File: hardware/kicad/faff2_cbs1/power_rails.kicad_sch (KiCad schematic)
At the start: 58 parts, among them U301 LMR33630, U302 TPS7A20, U303 TPS7A20, U304 LMR33630

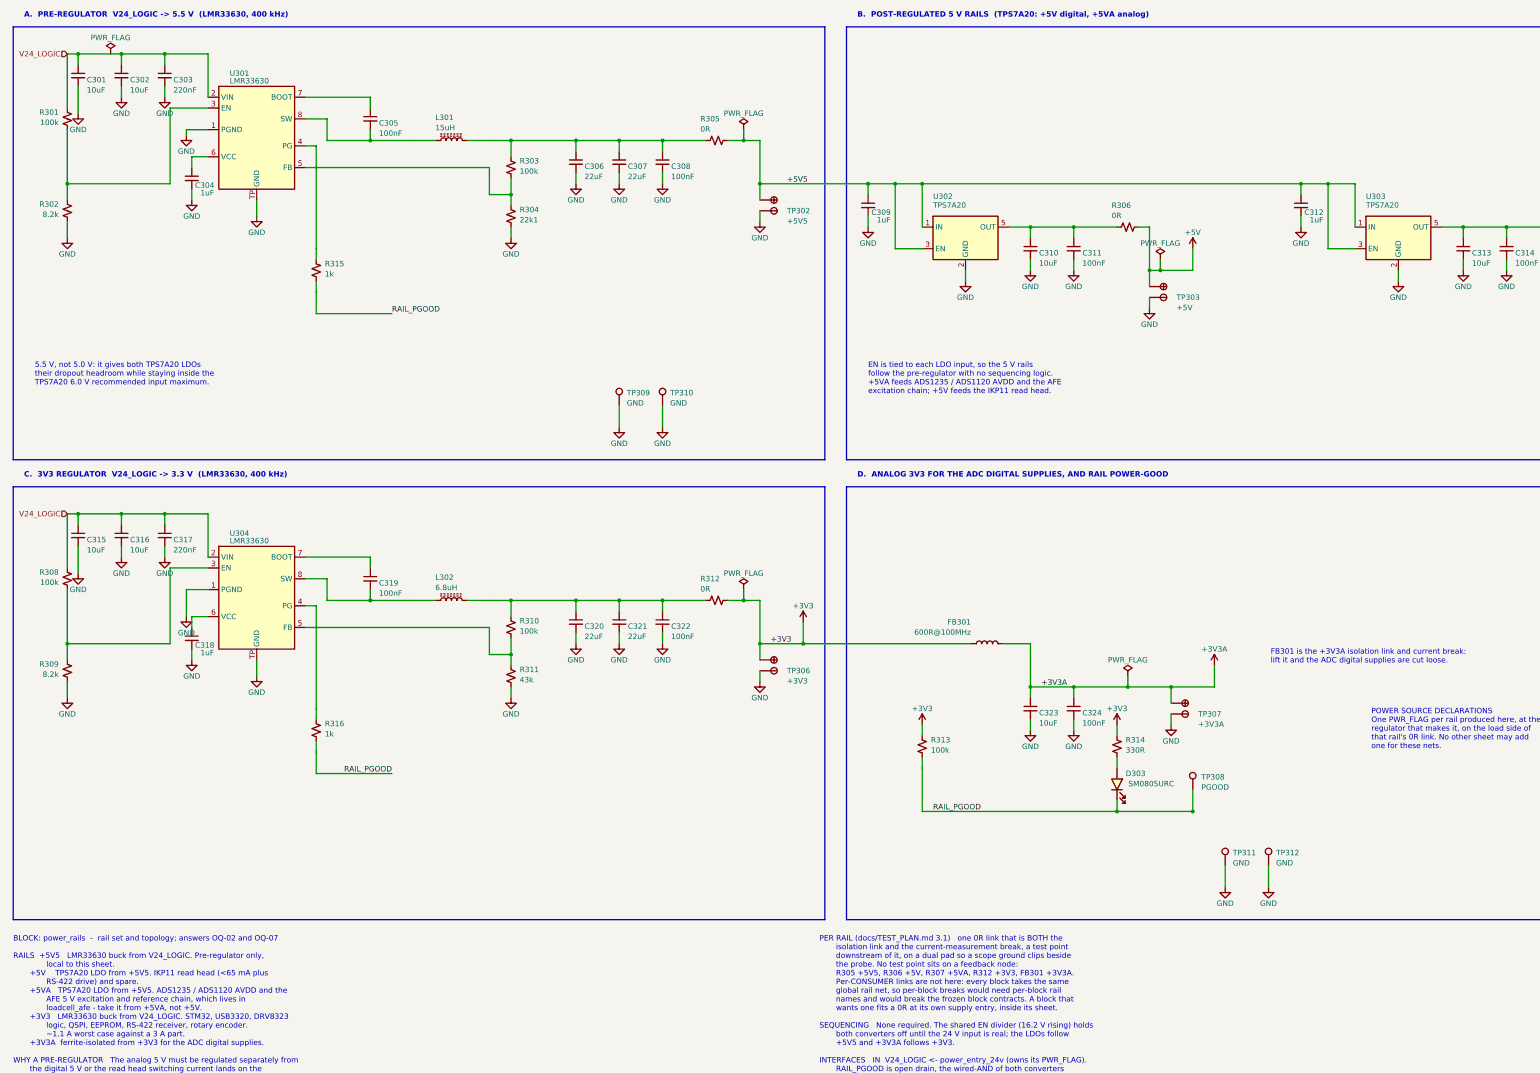
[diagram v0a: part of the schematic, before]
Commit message: review r3 item 3: both 5 V LDOs become ADPL42005ACPZ-5.0-R7
The captain overruled round 2's decision to keep the TPS7A20 - DEC-P3 asked to
be overruled, and was. The part was already in the house library, SymLifecycle
tested, with its LFCSP-8 footprint present, so nothing went project-local.

analog.com times out from this environment on two routes, so
datasheets/ADPL42005.pdf is a mirror of the same Rev. 0 document from
datasheetall.com, verified as a real PDF and parsed with pypdf; the README row
says so and asks for a vendor re-fetch. Nothing here is from memory.

Against Table 5: VIN and EN to +5V5 (the datasheet's own automatic-startup
connection), NC left bare, GND/GND/EPAD wired, VOUT bypassed, PG no-connect.
The three left-side ground pins land on a 2.54 row so they stub to one rail
ending in a single downward GND - schematic-style's dense-pin-row rule - and the
GND that hung under the SOT-23 became that rail's terminus.

SENSE goes to VOUT at the regulator, not past the 0R link. "As close as possible
to the load" argues for the far side of R306/R307, but those are TEST_PLAN 3.2
current-measurement breaks that get lifted on purpose, and sensing downstream
would open the loop the moment one came out. The datasheet's own specs are given
for "SENSE connected to VOUT", so this is the characterised configuration.

CIN 1uF -> 10uF is the only passive the datasheet forced: COUT needs >= 1uF at
<= 1 ohm ESR, and "if greater than 1uF of output capacitance is required, the
input capacitor should be increased to match it". COUT stays 10uF + 100nF
because a larger COUT improves transient response. C309/C312 use the 0805 25 V
part rather than the outputs' 0603 10 V one: they sit on the 5.5 V rail, where a
10 V X5R loses most of its capacitance to DC bias - the wrong way to satisfy a
"match COUT" requirement. The wider body pushed the Value 0.44 mm into the EN
wire, so its anchor now lines up with the Reference above it.

Two things for the captain, both in the decisions 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
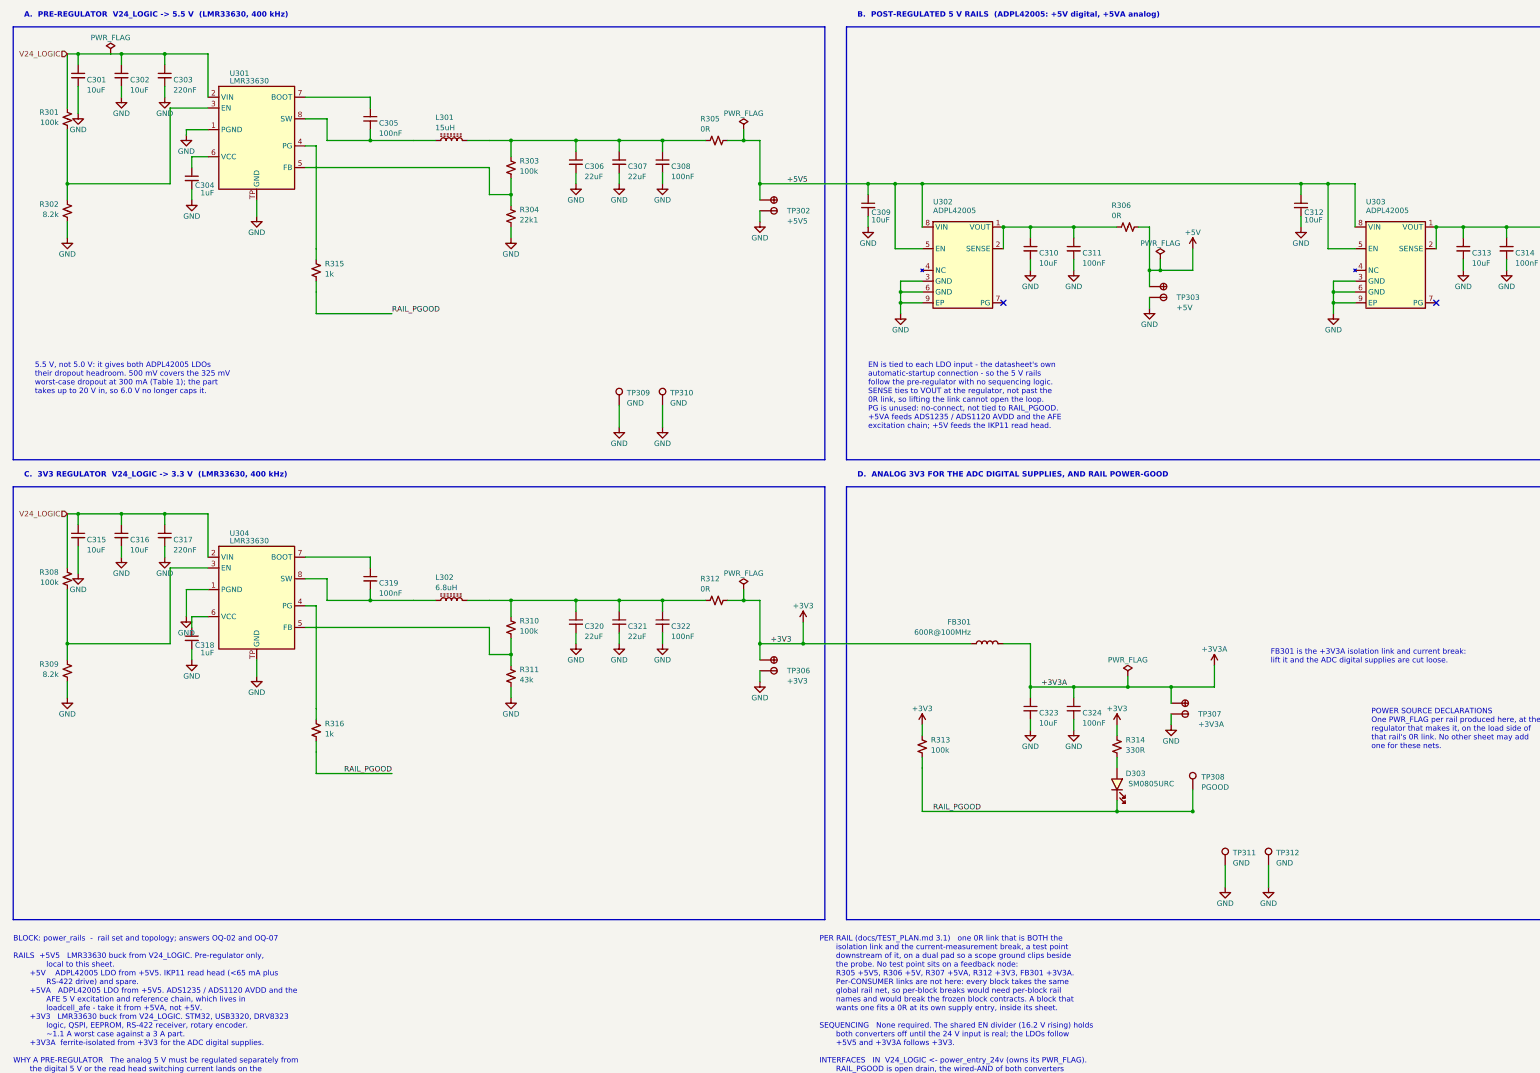
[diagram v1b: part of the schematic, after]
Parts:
- removed U302, U303: TPS7A20, Amodo:SOT23-5 - TI, symbol Amodo_Power_ICs:TPS7A2050PDBV
- added U302, U303: ADPL42005, Amodo:LFCSP-8 - 3x3mm body - 0.5mm pitch - 2.5x1.8mm EP, symbol Amodo_Power_ICs:ADPL42005ACPZ-5.0-R7
- C309, C312: value 1uF -> 10uF; symbol Amodo_Capacitors:CAP_MLCC_1uF_0603_10%_16V -> Amodo_Capacitors:CAP_MLCC_10uF_0805_20%_25V
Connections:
- net +5V5: now also U302.5 (EN), U302.8 (VIN), U303.5 (EN), U303.8 (VIN)
- net GND: now also U302.3 (GND), U302.6 (GND), U302.9 (EP), U303.3 (GND), U303.6 (GND), U303.9 (EP)
- net at C310.1, C311.1, R306.1: now also U302.1 (VOUT), U302.2 (SENSE)
- net at C313.1, C314.1, R307.1: now also U303.1 (VOUT), U303.2 (SENSE)
- no-connect marks 0 -> 2
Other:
- note added: "5.5 V, not 5.0 V: it gives both ADPL42005 LDOs their dropout headroom. 500 mV covers the 325 mV worst-case dropout at 300 mA (Table 1); the part takes up to 20 V in, so 6.0 V no longer caps it."
- note added: "B. POST-REGULATED 5 V RAILS (ADPL42005: +5V digital, +5VA analog)"
- note added: "BLOCK: power_rails - rail set and topology; answers OQ-02 and OQ-07 RAILS +5V5 LMR33630 buck from V24_LOGIC. Pre-regulator only, local to this sheet. +5V ADPL42005 LDO from +5V5. IKP11 read head (<65 mA plus RS-422 drive) and spare. +5VA ADPL42005 LDO from +5V5. ADS1235 / ADS1120 AVDD and the AFE 5 V excitation and reference chain, which lives in loadcell_afe - take it from +5VA, not +5V. +3V3 LM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"
- note added: "EN is tied to each LDO input - the datasheet's own automatic-startup connection - so the 5 V rails follow the pre-regulator with no sequencing logic. SENSE ties to VOUT at the regulator, not past the 0R link, so lifting the link cannot open the loop. PG is unused: no-connect, not tied to RAIL_PGOOD. +5VA feeds ADS1235 / ADS1120 AVDD and the AFE excitation chain; +5V feeds the IKP11 read head."
- note removed: "5.5 V, not 5.0 V: it gives both TPS7A20 LDOs their dropout headroom while staying inside the TPS7A20 6.0 V recommended input maximum."
- note removed: "B. POST-REGULATED 5 V RAILS (TPS7A20: +5V digital, +5VA analog)"
- note removed: "BLOCK: power_rails - rail set and topology; answers OQ-02 and OQ-07 RAILS +5V5 LMR33630 buck from V24_LOGIC. Pre-regulator only, local to this sheet. +5V TPS7A20 LDO from +5V5. IKP11 read head (<65 mA plus RS-422 drive) and spare. +5VA TPS7A20 LDO from +5V5. ADS1235 / ADS1120 AVDD and the AFE 5 V excitation and reference chain, which lives in loadcell_afe - take it from +5VA, not +5V. +3V3 LMR336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"
- note removed: "EN is tied to each LDO input, so the 5 V rails follow the pre-regulator with no sequencing logic. +5VA feeds ADS1235 / ADS1120 AVDD and the AFE excitation chain; +5V feeds the IKP11 read head."

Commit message: review r3 item 4: respace every grazing placement, and rehome the TIM1 note
Round 2 left thirteen power-symbol names grazing something and pinned the
labels. Item 1's checker turned thirteen into sixty once labels and bodies
became subjects and the font model learned that block titles are bold 1.778 -
40% wider per character than the 1.27 it had assumed, which is how a 35 mm
title came back as 25. Fifty-seven are now clear. ERC 0/0 and node sets
identical: every change here is geometry.

The dominant defect, ten times over, is a power symbol's arrow with a vertex
exactly on a wire that runs past it and does not connect - the same thing the
captain screenshotted, nine more times. Each moves along its own stub: GND
arrows up, rail arrows down, because a rail arrow's name sits above it and
moving up only puts the text where the arrow was.

The rest: six bold titles wider than their block, eight notes and labels running
out through a border, twelve pinned names overlapped by a neighbour that moved
instead, and both 5 V PWR_FLAGs, which move onto the test-point stub below where
their 9.5 mm name has clear air.

Two checker corrections came out of doing the work. Fourteen findings were text
over its OWN conductor - a label on its wire with a branch of the same net
dropping through the text, which is what "the wire must extend under the entire
label" asks for; wire_nodes() groups segments into electrical nodes and excuses
the whole node. And field-against-field comparison had been lost in the
subject/obstacle rewrite - reference-against-value is the commonest defect there
is, and it went unnoticed until a render showed PWR_FLAG 0.86 mm inside a
neighbouring 100nF on a sheet the checker called clean.

The TIM1 note: round 2 recorded that nothing 47.6 x 8.7 fitted anywhere in
motor_drive block 4. With item 1's geometry that was wrong - 495 positions fit.
It now sits beside U1101's logic inputs, which is what it describes.

Three are left, both explained in the decisions file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
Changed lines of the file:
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@@
 	(wire
 		(pts
-			(xy 27.94 63.5) (xy 52.07 63.5)
+			(xy 27.94 63.5) (xy 53.34 63.5)
 		)
 		(stroke
@@
 	(wire
 		(pts
-			(xy 27.94 171.45) (xy 52.07 171.45)
+			(xy 27.94 171.45) (xy 53.34 171.45)
 		)
 		(stroke
@@
 	(wire
 		(pts
-			(xy 52.07 45.72) (xy 52.07 63.5)
+			(xy 53.34 45.72) (xy 53.34 63.5)
 		)
 		(stroke
@@
 	(wire
 		(pts
-			(xy 52.07 45.72) (xy 60.96 45.72)
+			(xy 53.34 45.72) (xy 60.96 45.72)
 		)
 		(stroke
@@
 	(wire
 		(pts
-			(xy 52.07 153.67) (xy 52.07 171.45)
+			(xy 53.34 153.67) (xy 53.34 171.45)
 		)
 		(stroke
@@
 	(wire
 		(pts
-			(xy 52.07 153.67) (xy 60.96 153.67)
+			(xy 53.34 153.67) (xy 60.96 153.67)
 		)
 		(stroke
@@
 		)
 	)
+		(wire
+		(pts
+			(xy 281.94 83.82) (xy 292.1 83.82)
+		)
+		(stroke
+			(width 0)
+			(type default)
+		)
+	)
+	(wire
+		(pts
+			(xy 281.94 86.36) (xy 281.94 87.63)
+		)
+		(stroke
+			(width 0)
+			(type default)
+		)
+	)
+	(wire
+		(pts
+			(xy 275.59 86.36) (xy 281.94 86.36)
+		)
+		(stroke
+			(width 0)
+			(type default)
+		)
+	)
+		(wire
+		(pts
+			(xy 383.54 83.82) (xy 393.7 83.82)
+		)
+		(stroke
+			(width 0)
+			(type default)
+		)
+	)
+	(wire
+		(pts
+			(xy 383.54 86.36) (xy 383.54 87.63)
+		)
+		(stroke
+			(width 0)
+			(type default)
+		)
+	)
+	(wire
+		(pts
+			(xy 377.19 86.36) (xy 383.54 86.36)
+		)
+		(stroke
+			(width 0)
+			(type default)
+		)
+	)
+	(junction
+		(at 383.54 86.36)
+		(diameter 0)
+		(color 0 0 0 0)
+	)
+	(junction
+		(at 281.94 86.36)
+		(diameter 0)
+		(color 0 0 0 0)
+	)
 	(junction
 		(at 247.65 73.66)
@@
 	)
 	(rectangle
-		(start 15.24 26.67)
+		(start 13.97 26.67)
 		(end 205.74 128.27)
 		(stroke
@@
 	)
 	(rectangle
-		(start 15.24 134.62)
+		(start 13.97 134.62)
 		(end 205.74 236.22)
 		(stroke
@@
 	(wire
 		(pts
-			(xy 281.94 83.82) (xy 281.94 87.63)
+			(xy 281.94 83.82) (xy 281.94 86.36)
 		)
 		(stroke
@@
 	(wire
 		(pts
-			(xy 383.54 83.82) (xy 383.54 87.63)
+			(xy 383.54 83.82) (xy 383.54 86.36)
 		)
 		(stroke
@@
 	(wire
 		(pts
-			(xy 281.94 83.82) (xy 284.48 83.82)
-		)
-		(stroke
-			(width 0)
-			(type default)
-		)
-	)
-	(wire
-		(pts
-			(xy 284.48 83.82) (xy 292.1 83.82)
-		)
-		(stroke
-			(width 0)
-			(type default)
-		)
-	)
-	(wire
-		(pts
-			(xy 284.48 81.28) (xy 284.48 83.82)
-		)
-		(stroke
-			(width 0)
-			(type default)
-		)
-	)
-	(junction
-		(at 284.48 83.82)
-		(diameter 0)
-		(color 0 0 0 0)
-	)
-	(wire
-		(pts
-			(xy 383.54 83.82) (xy 386.08 83.82)
-		)
-		(stroke
-			(width 0)
-			(type default)
-		)
-	)
-	(wire
-		(pts
-			(xy 386.08 83.82) (xy 393.7 83.82)
-		)
-		(stroke
-			(width 0)
-			(type default)
-		)
-	)
-	(wire
-		(pts
-			(xy 386.08 81.28) (xy 386.08 83.82)
-		)
-		(stroke
-			(width 0)
-			(type default)
-		)
-	)
-	(junction
-		(at 386.08 83.82)
-		(diameter 0)
-		(color 0 0 0 0)
-	)
-	(wire
-		(pts
 			(xy 182.88 161.29) (xy 186.69 161.29)
 		)
@@
 			)
 		)
-	)	(symbol
+	)
+	(symbol
 		(lib_id "Amodo_Capacitors:CAP_MLCC_1uF_0603_10%_16V")
 		(at 57.15 62.23 0)
@@
 			)
 		)
-	)	(symbol
+	)
+	(symbol
 		(lib_id "Amodo_Symbols:GND")
 		(at 57.15 67.31 0)
@@
 			)
 		)
-	)	(symbol
+	)
+	(symbol
 		(lib_id "Amodo_Symbols:GND")
 		(at 72.39 71.12 0)
@@
 			)
 		)
-	)	(symbol
+	)
+	(symbol
 		(lib_id "Amodo_Inductors:IND_SMD_15uH_5.3A")
 		(at 118.11 53.34 0)
@@
 			)
 		)
-	)	(symbol
+	)
+	(symbol
 		(lib_id "Amodo_Resistors:RES_TNF_22.1k_0603_0.1%")
 		(at 132.08 68.58 0)
@@
 			)
 		)
-	)	(symbol
+	)
+	(symbol
 		(lib_id "Amodo_Resistors:RES_TF_1k_0603")
 		(at 86.36 81.28 0)
@@
 			)
 		)
-	)	(symbol
+	)
+	(symbol
 		(lib_id "Amodo_Symbols:GND")
 		(at 190.5 72.39 0)
@@
 			)
 		)
-	)	(symbol
+	)
+	(symbol
 		(lib_id "Amodo_Symbols:GND")
 		(at 281.94 92.71 0)
@@
 			)
 		)
-	)	(symbol
+	)
+	(symbol
 		(lib_id "Amodo_Symbols:GND")
 		(at 383.54 92.71 0)
@@
 			)
 		)
-	)	(symbol
+	)
+	(symbol
 		(lib_id "Amodo_Symbols:GND")
 		(at 190.5 180.34 0)
@@
 			)
 		)
-	)	(symbol
+	)
+	(symbol
 		(lib_id "Amodo_Symbols:GND")
 		(at 287.02 190.5 0)
@@
 			)
 		)
-	)	(symbol
+	)
+	(symbol
 		(lib_id "Amodo_Symbols:PWR_FLAG")
 		(at 38.1 33.02 0)
@@
 		)
 		(property "Value" "100nF"
-			(at 266.19 82.14 0)
+			(at 266.19 84.5 0)
 			(effects
 				(font
@@
 		)
 		(property "Value" "100nF"
-			(at 367.79 82.14 0)
+			(at 367.79 84.5 0)
 			(effects
 				(font
@@
 	(symbol
 		(lib_id "Amodo_Symbols:PWR_FLAG")
-		(at 284.48 81.28 0)
+		(at 275.59 86.36 0)
 		(unit 1)
 		(exclude_from_sim no)
@@
 		(fields_autoplaced no)
 		(property "Reference" "#FLG345"
-			(at 284.48 81.28 0)
+			(at 275.59 86.36 0)
 			(effects
 				(font
@@
 		)
 		(property "Value" "PWR_FLAG"
-			(at 284.48 77.47 0)
+			(at 275.59 82.55 0)
 			(effects
 				(font
@@
 		)
 		(property "Footprint" ""
-			(at 284.48 81.28 0)
+			(at 275.59 86.36 0)
 			(effects
 				(font
@@
 		)
 		(property "Datasheet" ""
-			(at 284.48 81.28 0)
+			(at 275.59 86.36 0)
 			(effects
 				(font
@@
 		)
 		(property "Description" "Special symbol for telling ERC where power comes from"
-			(at 284.48 81.28 0)
+			(at 275.59 86.36 0)
 			(effects
 				(font
@@
 		)
 		(property "SymLifecycle" "tested"
-			(at 284.48 81.28 0)
+			(at 275.59 86.36 0)
 			(effects
 				(font
@@
 		)
 		(property "ki_keywords" "flag power"
-			(at 284.48 81.28 0)
+			(at 275.59 86.36 0)
 			(effects
 				(font
@@
 	(symbol
 		(lib_id "Amodo_Symbols:PWR_FLAG")
-		(at 386.08 81.28 0)
+		(at 377.19 86.36 0)
 		(unit 1)
 		(exclude_from_sim no)
@@
 		(fields_autoplaced no)
 		(property "Reference" "#FLG347"
-			(at 386.08 81.28 0)
+			(at 377.19 86.36 0)
 			(effects
 				(font
@@
 		)
 		(property "Value" "PWR_FLAG"
-			(at 386.08 77.47 0)
+			(at 377.19 82.55 0)
 			(effects
 				(font
@@
 		)
 		(property "Footprint" ""
-			(at 386.08 81.28 0)
+			(at 377.19 86.36 0)
 			(effects
 				(font
@@
 		)
 		(property "Datasheet" ""
-			(at 386.08 81.28 0)
+			(at 377.19 86.36 0)
 			(effects
 				(font
@@
 		)
 		(property "Description" "Special symbol for telling ERC where power comes from"
-			(at 386.08 81.28 0)
+			(at 377.19 86.36 0)
 			(effects
 				(font
@@
 		)
 		(property "SymLifecycle" "tested"
-			(at 386.08 81.28 0)
+			(at 377.19 86.36 0)
 			(effects
 				(font
@@
 		)
 		(property "ki_keywords" "flag power"
-			(at 386.08 81.28 0)
+			(at 377.19 86.36 0)
 			(effects
 				(font
